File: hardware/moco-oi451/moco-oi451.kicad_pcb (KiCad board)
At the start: 2 copper layers, 0 parts

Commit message: OI451 routed
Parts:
- added C1: 1uF, Capacitor_SMD:C_0603_1608Metric, F.Cu at (147.5, 109.5)
- added C10: 100nF, Capacitor_SMD:C_0402_1005Metric, F.Cu at (145.4, 98.8)
- added C11: 100nF, Capacitor_SMD:C_0402_1005Metric, F.Cu at (138.0, 100.7)
- added C12: 12pF, Capacitor_SMD:C_0402_1005Metric, F.Cu at (133.2, 101.7)
- added C13: 12pF, Capacitor_SMD:C_0402_1005Metric, F.Cu at (134.5, 103.0)
- added C14: 47nF/100V, Capacitor_SMD:C_0603_1608Metric, F.Cu at (156.0, 106.0)
- added C15: 1uF/16V, Capacitor_SMD:C_0603_1608Metric, F.Cu at (158.0, 106.0)
- added C16: 1uF/6.3V, Capacitor_SMD:C_0603_1608Metric, F.Cu at (158.3, 94.5)
- added C17: 100nF/50V, Capacitor_SMD:C_0603_1608Metric, F.Cu at (159.5, 106.7)
- added C19: 10uF/50V, Capacitor_SMD:C_0805_2012Metric, F.Cu at (161.0, 109.3)
- added C2: 1uF, Capacitor_SMD:C_0603_1608Metric, F.Cu at (144.5, 109.5)
- added C20: 100nF/6.3V, Capacitor_SMD:C_0603_1608Metric, F.Cu at (150.2, 99.5)
- added C21: 22uF/16V, Capacitor_SMD:C_0805_2012Metric, F.Cu at (153.6, 106.0)
- added C22: 22pF, Capacitor_SMD:C_0603_1608Metric, F.Cu at (147.8, 104.0)
- added C23: 22pF, Capacitor_SMD:C_0603_1608Metric, F.Cu at (147.8, 102.5)
- added C24: 22pF, Capacitor_SMD:C_0603_1608Metric, F.Cu at (147.8, 101.0)
- added C25: 10uF/50V, Capacitor_SMD:C_0805_2012Metric, F.Cu at (158.0, 110.0)
- added C26: 10uF/50V, Capacitor_SMD:C_0805_2012Metric, F.Cu at (156.0, 110.0)
- added C27: 10uF/50V, Capacitor_SMD:C_0805_2012Metric, F.Cu at (152.0, 113.5)
- added C28: 10uF/50V, Capacitor_SMD:C_0805_2012Metric, F.Cu at (154.0, 113.5)
- added C29: 10uF/50V, Capacitor_SMD:C_0805_2012Metric, F.Cu at (158.0, 113.5)
- added C3: 100nF, Capacitor_SMD:C_0402_1005Metric, F.Cu at (135.2, 95.8)
- added C30: 10uF/50V, Capacitor_SMD:C_0805_2012Metric, F.Cu at (156.0, 113.5)
- added C32: 10uF/50V, Capacitor_SMD:C_0805_2012Metric, F.Cu at (150.0, 113.5)
- added C33: 10uF/50V, Capacitor_SMD:C_0805_2012Metric, F.Cu at (153.0, 110.5)
- added C35: 100nF, Capacitor_SMD:C_0603_1608Metric_Pad1.08x0.95mm_HandSolder, B.Cu at (150.0, 94.0)
- added C36: 10uF/50V, Capacitor_SMD:C_0805_2012Metric, B.Cu at (163.7, 102.0)
- added C37: 10uF/50V, Capacitor_SMD:C_0805_2012Metric, B.Cu at (163.7, 100.0)
- added C38: 10uF/50V, Capacitor_SMD:C_0805_2012Metric, B.Cu at (163.7, 98.0)
- added C4: 100nF, Capacitor_SMD:C_0402_1005Metric, F.Cu at (147.5, 96.7)
- added C5: 100nF, Capacitor_SMD:C_0402_1005Metric, F.Cu at (143.5, 89.0)
- added C6: 100nF, Capacitor_SMD:C_0402_1005Metric, F.Cu at (136.5, 96.5)
- added C7: 10nF, Capacitor_SMD:C_0402_1005Metric, F.Cu at (146.8, 97.4)
- added C8: 1uF, Capacitor_SMD:C_0402_1005Metric, F.Cu at (146.1, 98.1)
- added H1: MountingHole, MountingHole:MountingHole_2.2mm_M2_ISO14580, F.Cu at (130.0, 100.0)
- added H2: MountingHole, MountingHole:MountingHole_2.2mm_M2_ISO14580, F.Cu at (160.0, 117.3)
- added H3: MountingHole, MountingHole:MountingHole_2.2mm_M2_ISO14580, F.Cu at (160.0, 82.7)
- added J1: V+, moco:wire_3.2mm, F.Cu at (164.0, 113.0)
- added J2: V-, moco:wire_3.2mm, F.Cu at (164.0, 86.9)
- added J3: Serial, Connector_JST:JST_GH_SM03B-GHS-TB_1x03-1MP_P1.25mm_Horizontal, F.Cu at (133.8, 109.2)
- added J4: Serial, Connector_JST:JST_GH_SM03B-GHS-TB_1x03-1MP_P1.25mm_Horizontal, F.Cu at (140.8, 116.2)
- added J5: Debug, Connector_PinHeader_2.54mm:PinHeader_2x04_P2.54mm_Vertical, F.Cu at (134.4, 91.7)
- added J6: A, moco:wire_3.2mm, F.Cu at (167.5, 107.0)
- added J7: B, moco:wire_3.2mm, F.Cu at (169.0, 100.0)
- added J8: C, moco:wire_3.2mm, F.Cu at (167.5, 93.0)
- added L1: 47uH, Inductor_SMD:L_Taiyo-Yuden_MD-3030, F.Cu at (150.5, 106.8)
- added LD1: LED_BAGR, moco:RGB LED 1.6x1.6mm, F.Cu at (129.5, 96.0)
- added NT1: NetTie_2, NetTie:NetTie-2_SMD_Pad0.5mm, F.Cu at (148.1, 115.6)
- added R10: 330R, Resistor_SMD:R_0603_1608Metric, F.Cu at (151.0, 101.0)
- added R11: 10k/100mW, Resistor_SMD:R_0603_1608Metric, F.Cu at (153.9, 86.8)
- added R12: 10k, Resistor_SMD:R_0603_1608Metric, F.Cu at (152.4, 86.8)
- added R13: 10k, Resistor_SMD:R_0603_1608Metric, F.Cu at (150.9, 86.8)
- added R2: 1k, Resistor_SMD:R_0402_1005Metric, F.Cu at (132.0, 95.0)
- added R3: 5k, Resistor_SMD:R_0402_1005Metric, F.Cu at (132.0, 96.0)
- added R4: 1k, Resistor_SMD:R_0402_1005Metric, F.Cu at (132.0, 97.0)
- added R5: 22R, Resistor_SMD:R_0603_1608Metric, F.Cu at (150.5, 106.8)
- added R6: 5.1k, Resistor_SMD:R_0603_1608Metric, F.Cu at (153.5, 94.5)
- added R7: 5.1k, Resistor_SMD:R_0603_1608Metric, F.Cu at (160.0, 94.5)
- added R8: 330R, Resistor_SMD:R_0603_1608Metric, F.Cu at (151.0, 104.0)
- added R9: 330R, Resistor_SMD:R_0603_1608Metric, F.Cu at (151.0, 102.5)
- added SB1: SolderJumper_2_Open, Jumper:SolderJumper-2_P1.3mm_Open_RoundedPad1.0x1.5mm, F.Cu at (146.0, 111.5)
- added SB2: SolderJumper_2_Bridged, Jumper:SolderJumper-2_P1.3mm_Bridged_RoundedPad1.0x1.5mm, F.Cu at (144.6, 101.6)
- added SW1: RESET, Button_Switch_SMD:SW_SPST_TL3342, F.Cu at (145.0, 82.0)
- added SW2: DRV_RST, Button_Switch_SMD:SW_SPST_TL3342, F.Cu at (153.5, 82.0)
- added TP1: V_{CC}, TestPoint:TestPoint_Pad_D1.0mm, B.Cu at (143.2, 108.0)
- added TP2: V_{BK}, TestPoint:TestPoint_Pad_D1.0mm, B.Cu at (152.2, 106.6)
- added U1: RT9013-33GB, Package_TO_SOT_SMD:SOT-23-5, F.Cu at (146.0, 107.0)
- added U2: STM32G431CBUx, Package_DFN_QFN:QFN-48-1EP_7x7mm_P0.5mm_EP5.6x5.6mm, F.Cu at (141.5, 94.6)
- added U3: DRV8316CR, moco:VQFN-40_RGF_5x7mm_0.5mm_pitch_thermalpad, F.Cu at (157.4, 100.0)
- added U4: LM4040A50, Package_TO_SOT_SMD:SOT-353_SC-70-5, F.Cu at (156.2, 86.8)
- added U5: AS5047x, Package_SO:TSSOP-14_4.4x5mm_P0.65mm, B.Cu at (150.0, 100.0)
- added Y1: 8MHz, Crystal:Crystal_SMD_3225-4Pin_3.2x2.5mm, F.Cu at (135.5, 100.0)
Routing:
- net +3.3V: track 0.00 -> 86.2 mm, vias 0 -> 9
- net Vdrive: track 0.00 -> 72.1 mm, vias 0 -> 1
- net +5V: track 0.00 -> 69.0 mm, vias 0 -> 3
- net GND: track 0.00 -> 53.3 mm, vias 0 -> 45
- net /~{RESET}: track 0.00 -> 45.4 mm, vias 0 -> 2
- net /Driver/~{FAULT}: track 0.00 -> 44.0 mm, vias 0 -> 2
- net GNDPWR: track 0.00 -> 41.2 mm, vias 0 -> 45
- net /Driver/DRVOFF: track 0.00 -> 39.8 mm, vias 0 -> 2
- net / Rotary Sensor/MISO: track 0.00 -> 37.8 mm, vias 0 -> 2
- net / Rotary Sensor/MOSI: track 0.00 -> 36.3 mm, vias 0 -> 2
- net / Rotary Sensor/SCLK: track 0.00 -> 35.4 mm, vias 0 -> 2
- net /UART1_TX: track 0.00 -> 35.4 mm, vias 0 -> 2
- net /UART1_RX: track 0.00 -> 32.0 mm, vias 0 -> 1
- net /Driver/~{CS}: track 0.00 -> 31.6 mm, vias 0 -> 2
- net /Driver/~{SLEEP}: track 0.00 -> 25.4 mm
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- added copper zone on F.Cu, net /Driver/OUTA
- added copper zone on F.Cu, net /Driver/OUTB
- added copper zone on F.Cu, net /Driver/OUTC
- added copper zone on B.Cu, net GND
- added copper zone on F.Cu, net GND
- added copper zone on B.Cu, net GNDPWR
- added copper zone on F.Cu, net GNDPWR
- added copper zone on F.Cu, net Vdrive
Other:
- board outline added: 45 x 45 mm
- board text added: "0.1300 mm / 0.1300 mm"
- board text added: "0.3000 mm"
- board text added: "1.6000 mm"
- board text added: "2"
- board text added: "44.9950 mm x 44.9975 mm"
- board text added: "BOARD CHARACTERISTICS"
- board text added: "Board Thickness:"
- board text added: "Board overall dimensions:"
- board text added: "Castellated pads:"
- board text added: "Copper Finish:"
- board text added: "Copper Layer Count:"
- board text added: "Edge card connectors:"
- board text added: "Impedance Control:"
- board text added: "Min hole diameter:"
- board text added: "Min track/spacing:"
- board text added: "No"
- board text added: "None"
- board text added: "Plated Board Edge:"

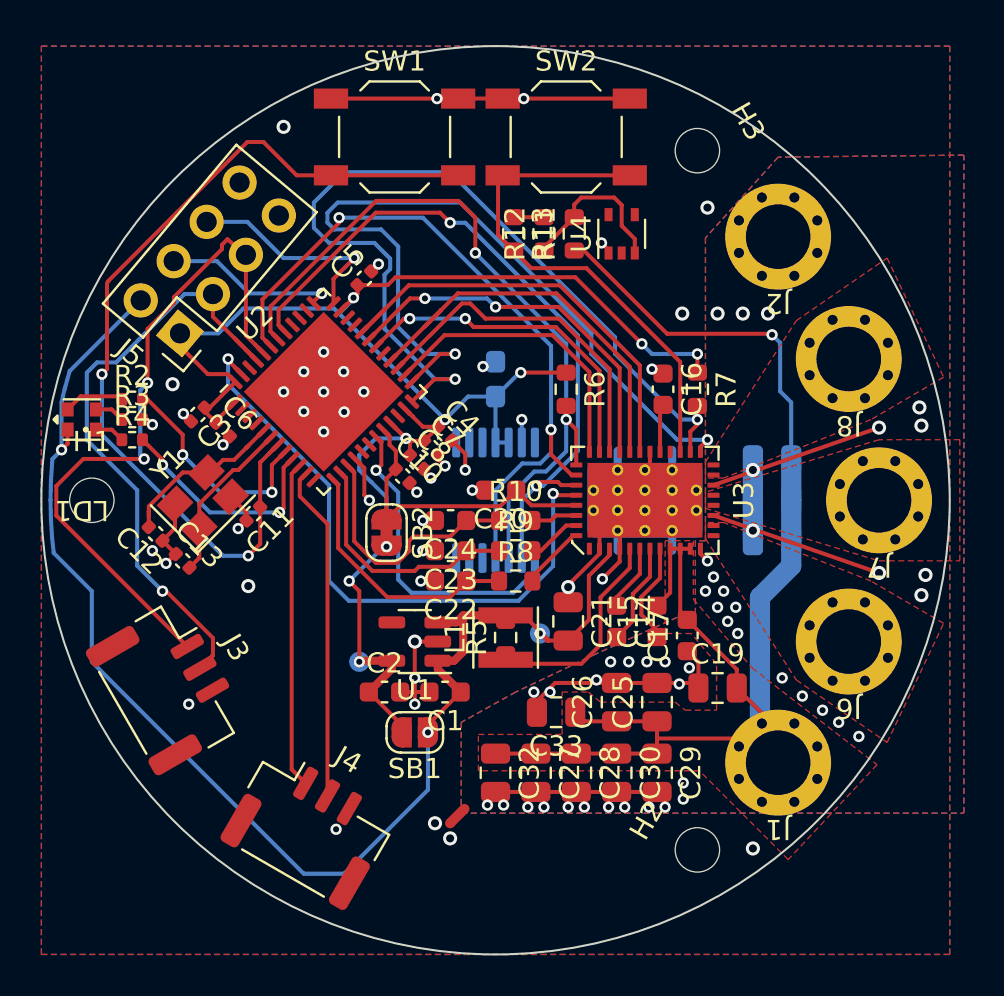
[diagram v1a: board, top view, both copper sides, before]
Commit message: Reroute and reduce size to Ø40mm
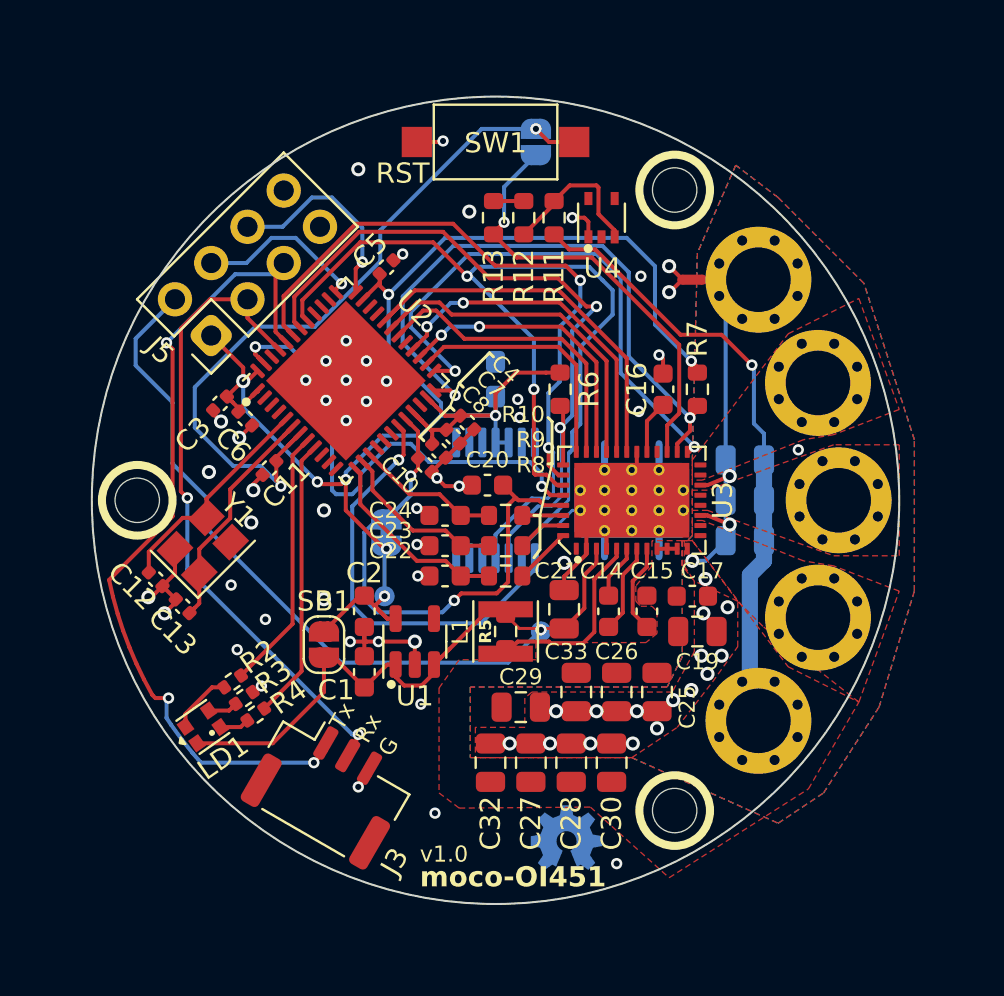
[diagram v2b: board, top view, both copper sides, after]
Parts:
- removed J4: Serial, Connector_JST:JST_GH_SM03B-GHS-TB_1x03-1MP_P1.25mm_Horizontal
- removed SW2: DRV_RST, Button_Switch_SMD:SW_SPST_TL3342
- added SB3: SolderJumper_2_Open, Jumper:SolderJumper-2_P1.3mm_Open_RoundedPad1.0x1.5mm, B.Cu at (152.0, 82.2)
- SB2: moved to B.Cu
- SW1: footprint Button_Switch_SMD:SW_SPST_TL3342 -> Button_Switch_SMD:SW_SPST_CK_RS282G05A3
- moved H2 32.7 mm to (158.9, 84.6), turned to 120 degrees
- moved H3 32.7 mm to (158.9, 115.4), turned to -120 degrees
- moved NT1 29.0 mm to (159.8, 89.1), turned to 180 degrees
- moved LD1 16.4 mm to (135.5, 111.2), turned to -145 degrees
- moved R4 14.9 mm to (138.1, 110.6), turned to 35 degrees
- moved R3 14.9 mm to (137.5, 109.8), turned to 35 degrees
- moved R2 14.8 mm to (137.0, 109.0), turned to 35 degrees
- moved J3 9.43 mm to (141.8, 114.2), turned to -30 degrees
- moved C29 7.49 mm to (151.2, 110.2), turned to 0 degrees
- moved SB1 6.26 mm to (141.5, 107.2), turned to 90 degrees
- moved SW1 5.01 mm to (150.0, 82.2)
- moved C1 4.12 mm to (143.5, 108.5), turned to 90 degrees
- moved C2 4.12 mm to (143.5, 105.5), turned to -90 degrees
- moved TP1 3.48 mm to (144.5, 104.8)
- moved C19 2.97 mm to (160.0, 106.5), turned to 180 degrees
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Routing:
- net Vdrive: track 72.1 -> 31.8 mm
- net GNDPWR: track 41.2 -> 19.0 mm, vias 45 -> 20
- net /UART2_RX: track 16.7 -> 0.00 mm
- net /UART2_TX: track 16.2 -> 0.00 mm
- net /Driver/~{FAULT}: track 44.0 -> 31.0 mm
- net /Driver/DRVOFF: track 39.8 -> 27.3 mm
- net / Rotary Sensor/SCLK: track 35.4 -> 47.2 mm
- net GND: track 53.3 -> 42.0 mm, vias 45 -> 47
- net /Driver/V_{REF}: track 15.2 -> 26.3 mm, vias 0 -> 2
- net /~{RESET}: track 45.4 -> 36.8 mm
- net /UART1_TX: track 35.4 -> 42.6 mm, vias 2 -> 3
- net /Driver/~{CS}: track 31.6 -> 25.7 mm
- net / Rotary Sensor/~{CS}: track 15.9 -> 21.7 mm
- net /Driver/SOC: track 12.9 -> 7.14 mm
- net /Driver/SOB: track 12.5 -> 8.51 mm
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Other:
- board size 45 x 45 mm -> 40 x 40 mm
- board text added: "${TITLE}"
- board text added: "+"
- board text added: "+10~35V"
- board text added: "-"
- board text added: "3.3V"
- board text added: "3xM2 P.C.D Ø35.5"
- board text added: "5V"
- board text added: "A"
- board text added: "B"
- board text added: "C"
- board text added: "GND"
- board text added: "Rx"
- board text added: "SWC"
- board text added: "SWD"
- board text added: "Tx"
- board text added: "v${REVISION}"
- board text removed: "0.1300 mm / 0.1300 mm"
- board text removed: "0.3000 mm"
- board text removed: "1.6000 mm"
- board text removed: "2"
- board text removed: "44.9950 mm x 44.9975 mm"
- board text removed: "BOARD CHARACTERISTICS"
- board text removed: "Board Thickness:"
- board text removed: "Board overall dimensions:"
- board text removed: "Castellated pads:"
- board text removed: "Copper Finish:"
- board text removed: "Copper Layer Count:"
- board text removed: "Edge card connectors:"
- board text removed: "Impedance Control:"
- board text removed: "Min hole diameter:"
- board text removed: "Min track/spacing:"
- board text removed: "No"
- board text removed: "None"
- board text removed: "Plated Board Edge:"

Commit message: Optimize routing
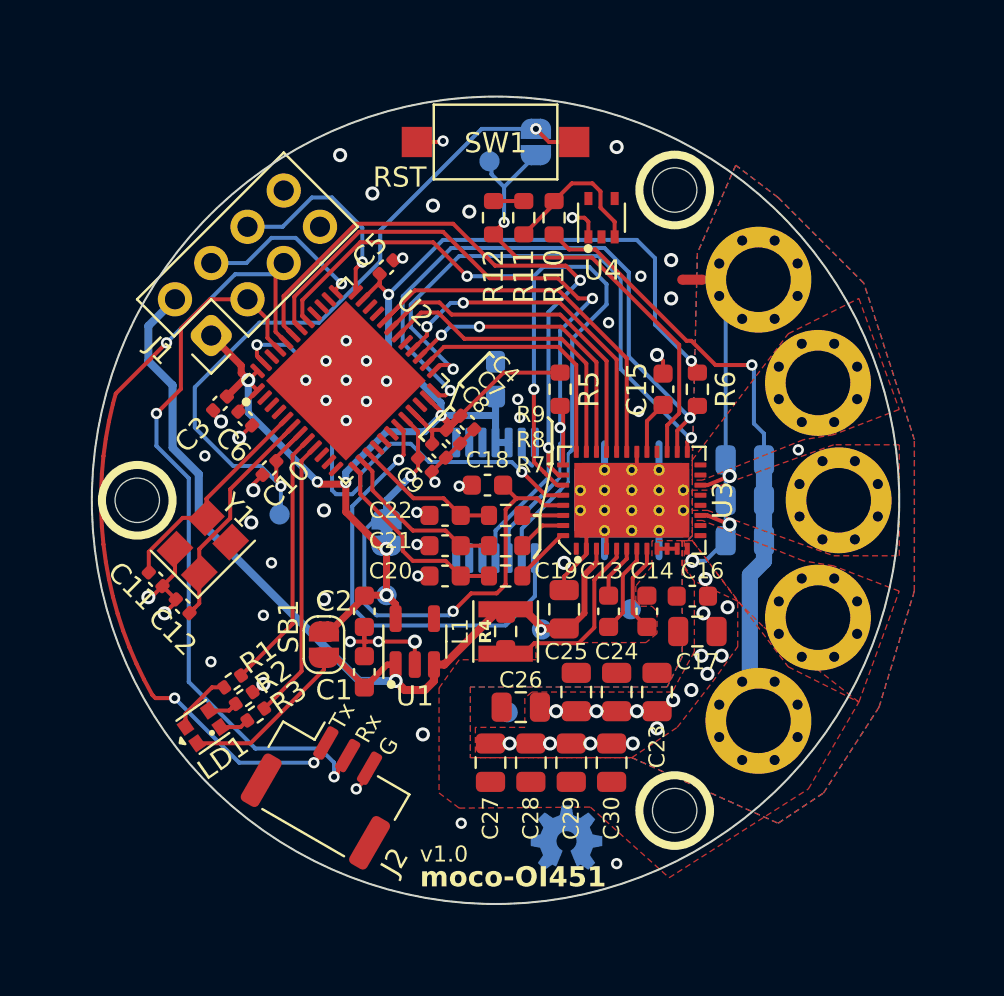
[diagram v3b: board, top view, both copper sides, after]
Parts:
- removed the TP2 at (152.2, 106.5)
- added TP1: ~{RESET}, TestPoint:TestPoint_Pad_D1.0mm, B.Cu at (139.3, 100.7)
- added TP3: GND, TestPoint:TestPoint_Pad_D1.0mm, B.Cu at (156.7, 105.4)
- added TP4: V_{BK}, TestPoint:TestPoint_Pad_D1.0mm, B.Cu at (152.3, 106.4)
- added TP5: PGND, TestPoint:TestPoint_Pad_D1.0mm, B.Cu at (150.6, 110.5)
- added TP6: nSLEEP, TestPoint:TestPoint_Pad_D1.0mm, B.Cu at (149.7, 83.2)
- moved TP2 0.11 mm to (144.6, 104.7)
- renumbered C11 to C10, C12 to C11, C13 to C12, C14 to C13, C15 to C14, C16 to C15, C17 to C16, C19 to C17, C20 to C18, C21 to C19, C22 to C20, C23 to C21, C24 to C22, C25 to C23, C26 to C24, C33 to C25, C29 to C26, C32 to C27, C27 to C28, C28 to C29, C36 to C31, C37 to C32, C38 to C33, C35 to C34, C10 to C9, J5 to J1, J3 to J2, J1 to J3, J2 to J4, J6 to J5, J7 to J6, J8 to J7, R2 to R1, R11 to R10, R12 to R11, R13 to R12, R3 to R2, R4 to R3, R5 to R4, R6 to R5, R7 to R6, R8 to R7, R9 to R8, R10 to R9, SB3 to SB2, SB2 to SB3, TP1 to TP2
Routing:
- net +5V: track 65.5 -> 55.7 mm, vias 1 -> 2
- net /UART1_RX: track 32.2 -> 36.6 mm
- net GND: track 42.0 -> 39.4 mm, vias 47 -> 51
- net / Rotary Sensor/SCLK: track 47.2 -> 45.2 mm
- net /Driver/~{SLEEP}: track 21.8 -> 23.4 mm
- net /~{RESET}: track 36.8 -> 38.2 mm
- net /UART1_TX: track 42.6 -> 41.3 mm
- net / Rotary Sensor/MOSI: track 37.8 -> 37.1 mm
- net /Driver/~{FAULT}: track 31.0 -> 30.5 mm
- net Net-(U3-SW_BK): track 9.80 -> 9.29 mm
